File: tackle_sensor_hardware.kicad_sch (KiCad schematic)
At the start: 78 parts, among them J1 Conn_01x02_Male, J2 Conn_01x04_Male, J3 Conn_01x03_Male, J4 Conn_ARM_JTAG_SWD_10, Q1 DMP4051LK3, Q2 2N7002K, Q3 2N7002K, Q4 2N7002K, Q5 2N7002K, Q6 2N7002K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

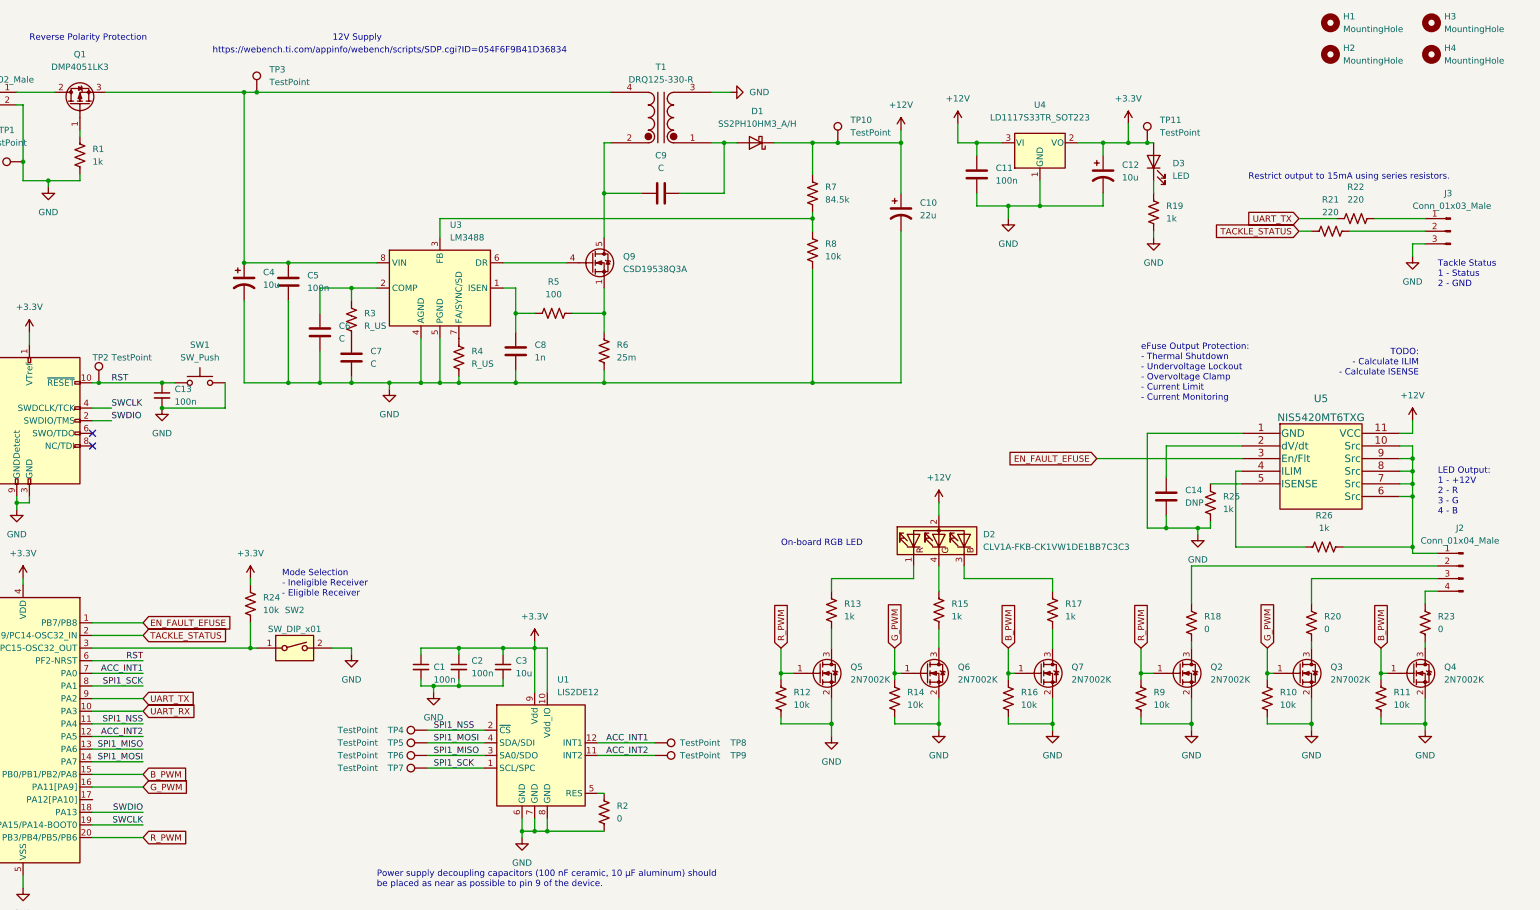
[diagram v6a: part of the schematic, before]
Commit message: Picked most RC components and footprints
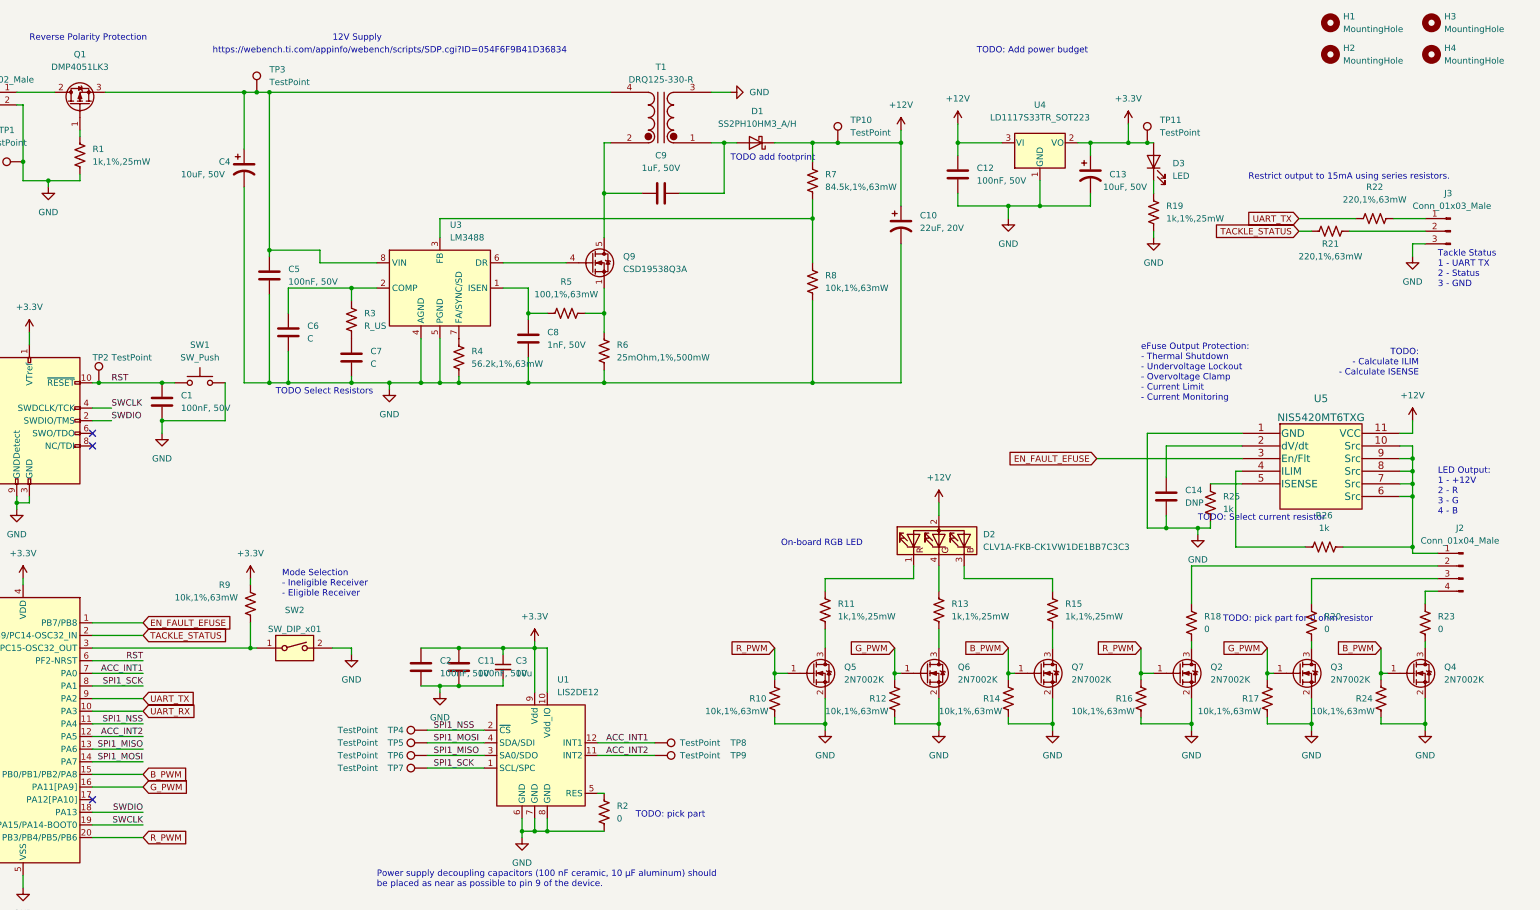
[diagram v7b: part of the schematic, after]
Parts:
- removed C1, C13, C2: 100n, Capacitor_SMD:C_0603_1608Metric, symbol Device:C_Small
- removed C12: 10u, symbol Device:C_Polarized_US
- added C1, C12, C2: 100nF, 50V, Capacitor_SMD:C_0805_2012Metric, symbol Device:C
- added C13: 10uF, 50V, Capacitor_SMD:CP_Elec_6.3x5.8, symbol Device:C_Polarized_US
- C10: value 22u -> 22uF, 20V; footprint (none) -> Capacitor_SMD:CP_Elec_6.3x5.9; MPN (none) -> 20SVP22M
- C11, C5: value 100n -> 100nF, 50V; footprint (none) -> Capacitor_SMD:C_0805_2012Metric; MPN (none) -> CC0805KRX7R9BB104
- C14: footprint (none) -> Capacitor_SMD:C_0402_1005Metric
- C4: value 10u -> 10uF, 50V; footprint (none) -> Capacitor_SMD:CP_Elec_6.3x5.8; MPN (none) -> UUD1H100MCL1GS
- C8: value 1n -> 1nF, 50V; footprint (none) -> Capacitor_SMD:C_0402_1005Metric; MPN (none) -> GRM1555C1H102JA01J
- C9: value C -> 1uF, 50V; footprint (none) -> Capacitor_SMD:C_0603_1608Metric; MPN (none) -> C1608X5R1H105K080AB
- D1, TP1, TP10, TP11, TP2, TP3, TP4, TP5, TP6, TP7, TP8, TP9: footprint (none) -> TestPoint:TestPoint_Pad_D1.5mm
- R1, R13, R15, R19: value 1k -> 1k,1%,25mW; MPN (none) -> ERJ-PA3F1001V
- R10, R12, R14, R16, R24, R9: value 10k -> 10k,1%,63mW; footprint Resistor_SMD:R_0603_1608Metric -> Resistor_SMD:R_0402_1005Metric
- R11: value 10k -> 1k,1%,25mW; MPN (none) -> ERJ-PA3F1001V
- R17: value 1k -> 10k,1%,63mW; footprint Resistor_SMD:R_0603_1608Metric -> Resistor_SMD:R_0402_1005Metric
- R21, R22: value 220 -> 220,1%,63mW; footprint Resistor_SMD:R_0603_1608Metric -> Resistor_SMD:R_0402_1005Metric; MPN (none) -> RC0402FR-07220RL
- R4: value R_US -> 56.2k,1%,63mW; footprint Resistor_SMD:R_0603_1608Metric -> Resistor_SMD:R_0402_1005Metric; MPN (none) -> RC0402FR-0756K2L
- R5: value 100 -> 100,1%,63mW; footprint Resistor_SMD:R_0603_1608Metric -> Resistor_SMD:R_0402_1005Metric; MPN (none) -> RC0402FR-07100RL
- R6: value 25m -> 25mOhm,1%,500mW; footprint Resistor_SMD:R_0603_1608Metric -> Resistor_SMD:R_1206_3216Metric; MPN (none) -> CSR1206FK25L0
- R7: value 84.5k -> 84.5k,1%,63mW; footprint (none) -> Resistor_SMD:R_0402_1005Metric; MPN (none) -> RMCF0402FT84K5
- R8: value 10k -> 10k,1%,63mW; footprint (none) -> Resistor_SMD:R_0402_1005Metric
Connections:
- net +12V: now also C12.1; no longer C11.1
- net +3V3: now also C11.1, R9.1, C13.1, C2.1; no longer R24.1
- net B_PWM: now also R14.1, R24.1; no longer R11.1, R16.1
- net GND: now also R17.2, R24.2, C1.2, C12.2, C13.2, C2.2; no longer R11.2, R9.2
- net G_PWM: now also R12.1, R17.1; no longer R10.1, R14.1
- net RST: now also C1.1
- net R_PWM: now also R10.1, R16.1; no longer R12.1, R9.1
- net at Q7.3 (D): now also R15.2; no longer R17.2
- net at SW2.1, U2.3 (PC15-OSC32_OUT): now also R9.2; no longer R24.2
- net at R13.1: now also D2.4 (BK); no longer D2.1 (A)
- net at D2.3 (GK): now also R15.1; no longer R17.1
- net at R13.2: now also Q6.3 (D); no longer Q5.3 (D)
- new net: D2.1 (A), R11.1
- new net: Q5.3 (D), R11.2
- no-connect marks 2 -> 3
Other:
- note added: "TODO Select Resistors"
- note added: "TODO add footprint"
- note added: "TODO: Add power budget"
- note added: "TODO: Select current resistor"
- note added: "TODO: pick part"
- note added: "TODO: pick part for 0 ohm resistor"
- note added: "Tackle Status 1 - UART TX 2 - Status 3 - GND"
- note removed: "Tackle Status 1 - Status 2 - GND"
- moved on the sheet: C10, C4, C5, C6, C8, Q5, R5, R7, R8

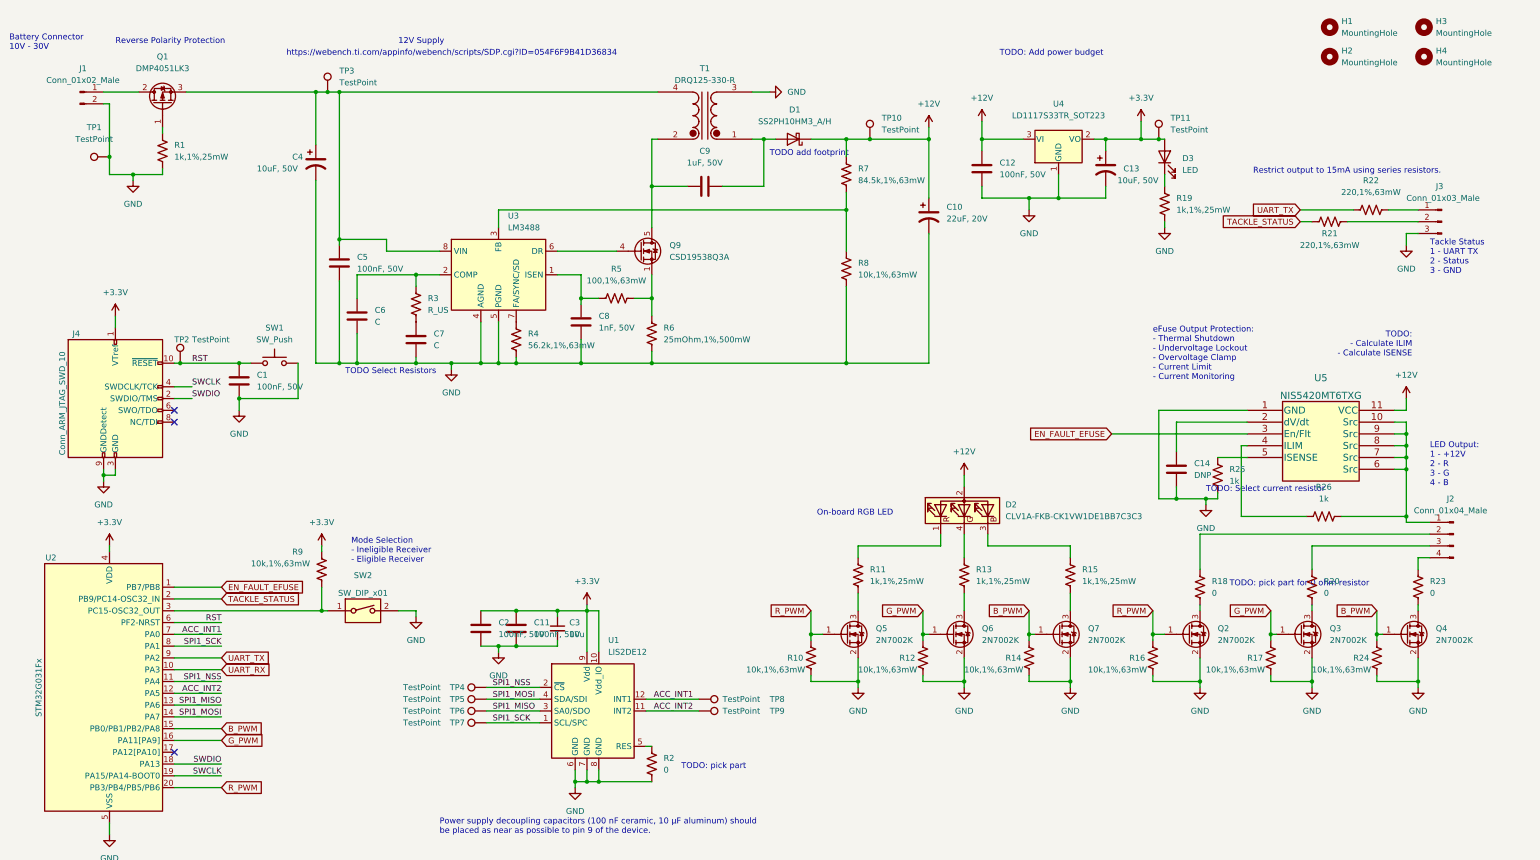
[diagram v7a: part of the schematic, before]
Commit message: updated component placement and board size, cleaning up schamtic and part selection.
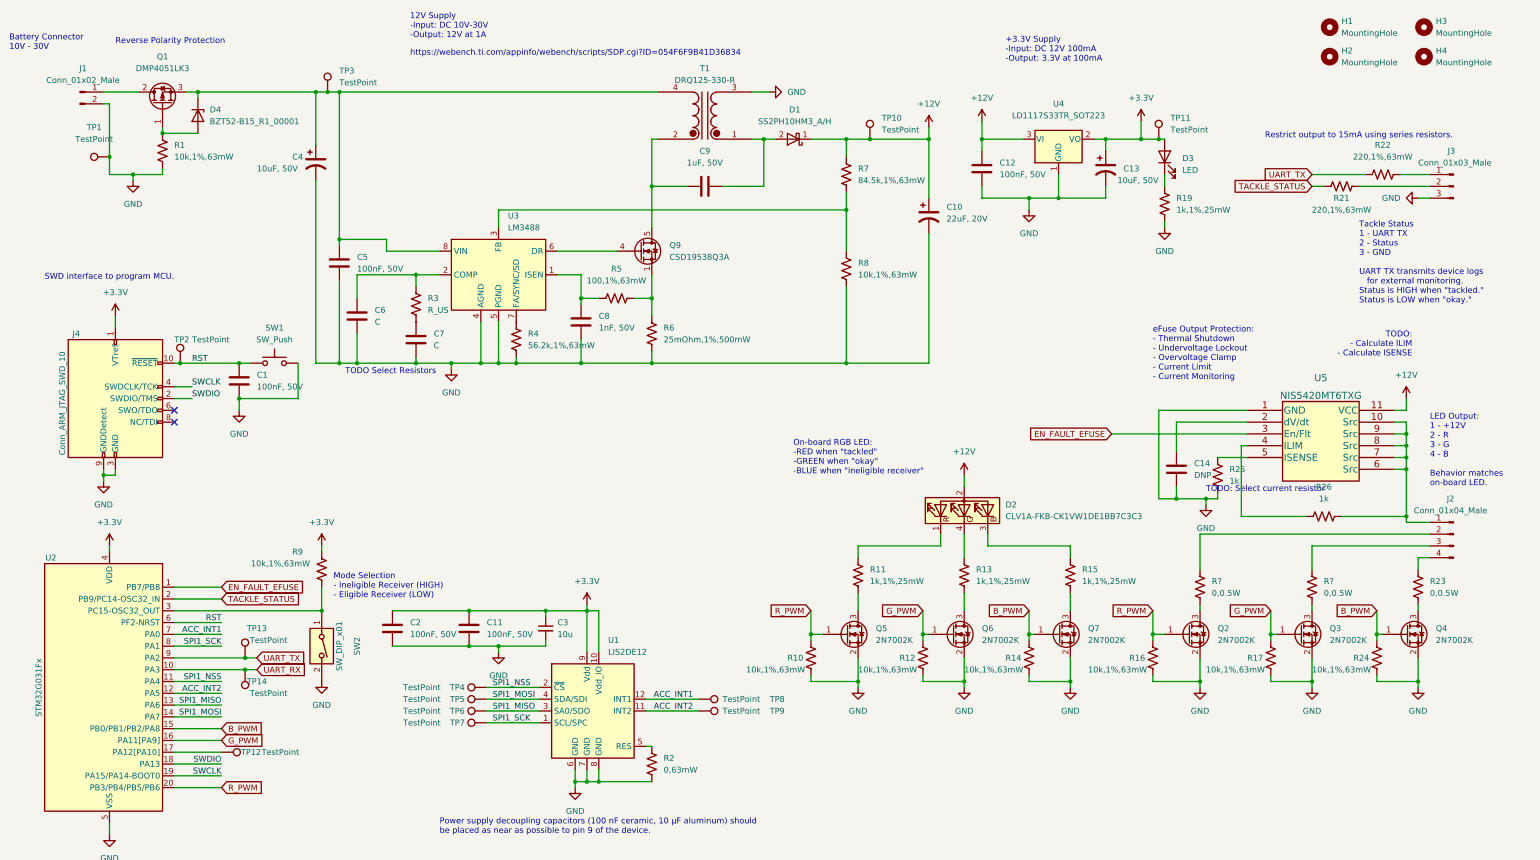
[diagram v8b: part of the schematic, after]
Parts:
- removed R18, R20: 0, Resistor_SMD:R_1210_3225Metric, symbol Device:R_US
- added D4: BZT52-B15_R1_00001, Diode_SMD:D_SOD-123, symbol Diode:BZT52Bxx
- added R? (x2): 0,0.5W, Resistor_SMD:R_1210_3225Metric, symbol Device:R_US
- added TP12, TP13, TP14: TestPoint, TestPoint:TestPoint_Pad_D1.5mm, symbol Connector:TestPoint
- D1: footprint TestPoint:TestPoint_Pad_D1.5mm -> Diode_SMD:D_Powermite_AK
- R1: value 1k,1%,25mW -> 10k,1%,63mW; footprint Resistor_SMD:R_0603_1608Metric -> Resistor_SMD:R_0402_1005Metric; MPN ERJ-PA3F1001V -> (none)
- R2: value 0 -> 0,63mW; footprint Resistor_SMD:R_0603_1608Metric -> Resistor_SMD:R_0402_1005Metric; MPN (none) -> RMCF0402ZT0R00
- R23: value 0 -> 0,0.5W; MPN (none) -> RMCF1210ZT0R00
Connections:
- net UART_RX: now also TP14.1
- net UART_TX: now also TP13.1
- net at C4.1, C5.1, Q1.3 (S)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: now also D4.1 (K)
- net at Q1.1 (G), R1.1: now also D4.2 (A)
- net at Q2.3 (D): now also R?.1
- net at U2.17 (PA12[PA10]): now also TP12.1
- net at J2.2 (Pin_2): now also R?.2
- net at J2.3 (Pin_3): now also R?.2
- net at Q3.3 (D): now also R?.1
- no-connect marks 3 -> 2
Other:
- note added: "+3.3V Supply -Input: DC 12V 100mA -Output: 3.3V at 100mA"
- note added: "12V Supply -Input: DC 10V-30V -Output: 12V at 1A"
- note added: "LED Output: 1 - +12V 2 - R 3 - G 4 - B Behavior matches on-board LED."
- note added: "Mode Selection - Ineligible Receiver (HIGH) - Eligible Receiver (LOW)"
- note added: "On-board RGB LED: -RED when "tackled" -GREEN when "okay" -BLUE when "ineligible receiver""
- note added: "SWD interface to program MCU."
- note added: "Tackle Status 1 - UART TX 2 - Status 3 - GND UART TX transmits device logs for external monitoring. Status is HIGH when "tackled." Status is LOW when "okay.""
- note removed: "12V Supply"
- note removed: "LED Output: 1 - +12V 2 - R 3 - G 4 - B"
- note removed: "Mode Selection - Ineligible Receiver - Eligible Receiver"
- note removed: "On-board RGB LED"
- note removed: "TODO add footprint"
- note removed: "TODO: Add power budget"
- note removed: "TODO: pick part"
- note removed: "TODO: pick part for 0 ohm resistor"
- note removed: "Tackle Status 1 - UART TX 2 - Status 3 - GND"
- moved on the sheet: C11, C2, C3, J3, R21, R22, SW2
